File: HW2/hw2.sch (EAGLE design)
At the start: 22 parts, among them J1 USB-MINIB-5P

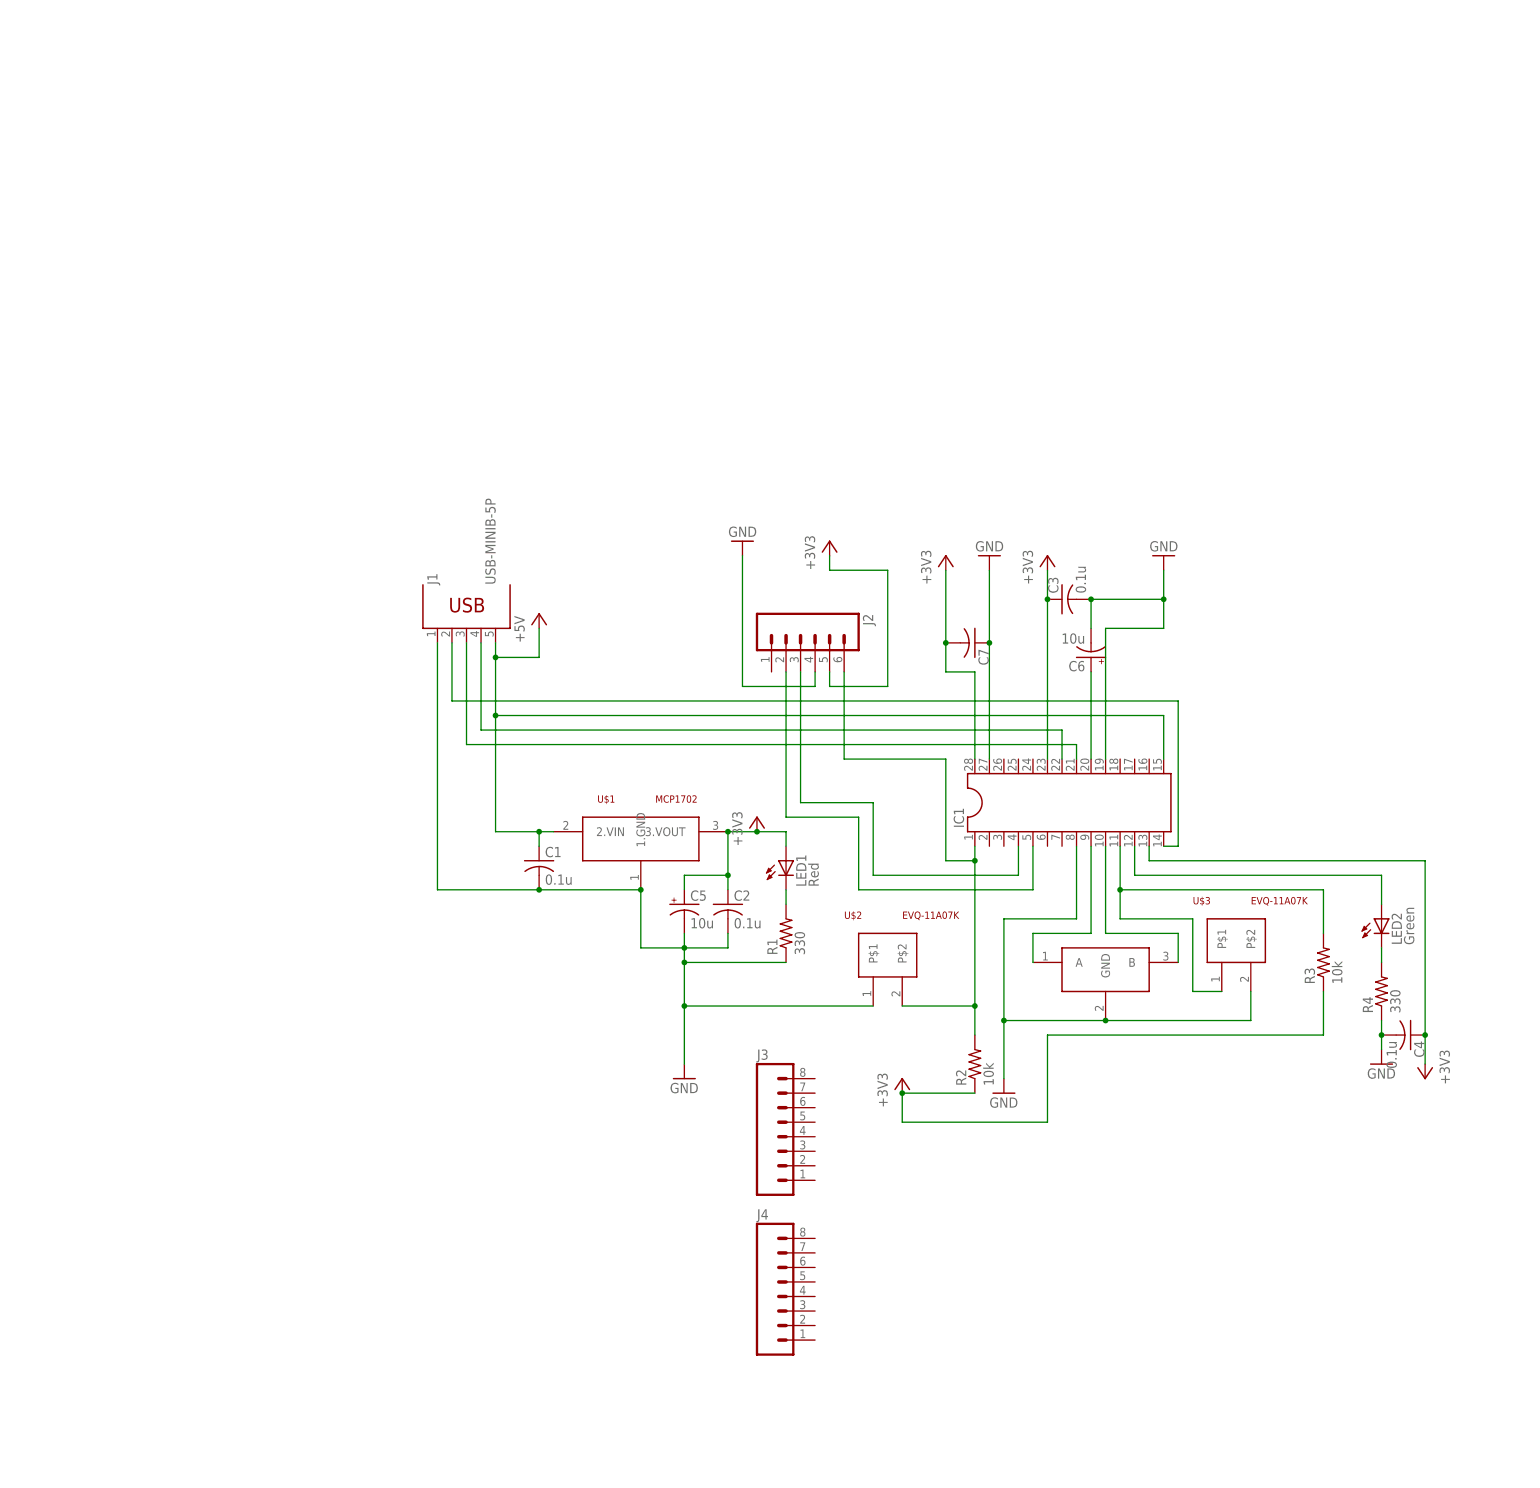
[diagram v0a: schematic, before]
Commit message: new schematic and library
The schematic has been improved.
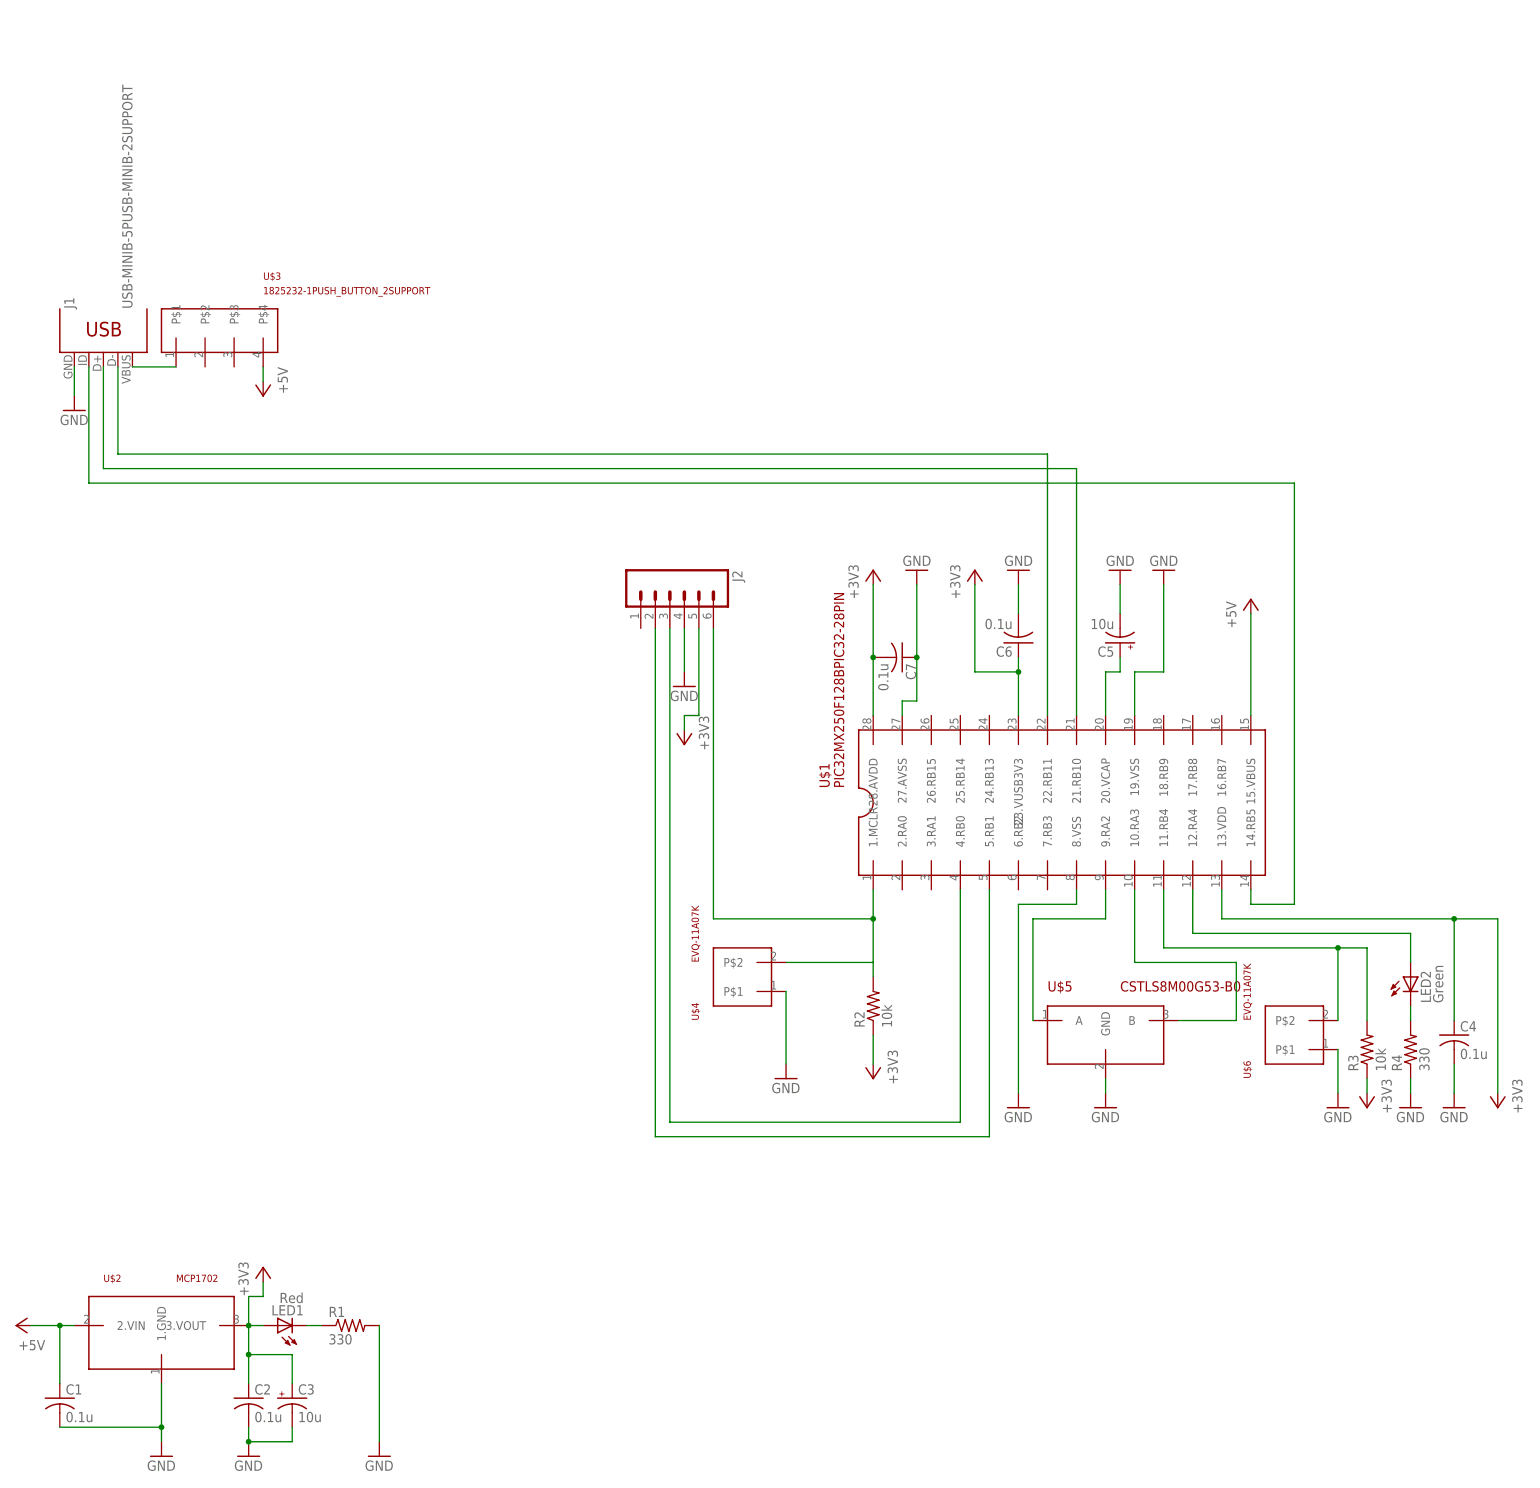
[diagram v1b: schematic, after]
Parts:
- removed IC1: (no value), hw2:DIL28-3
- removed J3, J4: (no value), hw2:M08
- added U$5: CSTLS8M00G53-B0, hw2:CSTLS8M00G53-B0
- added U$6: EVQ-11A07K, hw2:EVQ-11A07K
- C3: value 0.1u -> 10u; device hw2:C-US025-025X050 -> hw2:CPOL-USB45181A
- C6: value 10u -> 0.1u; device hw2:CPOL-USB45181A -> hw2:C-US025-025X050
- C7: value (none) -> 0.1u
- J1: value USB-MINIB-5P -> USB-MINIB-5PUSB-MINIB-2SUPPORT; device hw2:USB-MINIB-5P -> hw2:USB-MINIB-5PUSB-MINIB-2SUPPORT
- J2: device hw2:M06NO_SILK_YES_STOP -> hw2:M06SILK_FEMALE_PTH
- U$1: value MCP1702 -> PIC32MX250F128BPIC32-28PIN; device hw2:MCP1702 -> hw2:PIC32MX250F128BPIC32-28PIN
- U$2: value EVQ-11A07K -> MCP1702; device hw2:EVQ-11A07K -> hw2:MCP1702
- U$3: value EVQ-11A07K -> 1825232-1PUSH_BUTTON_2SUPPORT; device hw2:EVQ-11A07K -> hw2:1825232-1PUSH_BUTTON_2SUPPORT
- U$4: value CSTLS8M00G53-B0 -> EVQ-11A07K; device hw2:CSTLS8M00G53-B0 -> hw2:EVQ-11A07K
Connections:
- removed net N$15: IC1.10, U$4.B
- removed net N$16: IC1.11, R3.2, U$3.P$1
- removed net N$19: IC1.12, LED2.A
- new net N$1: J1.ID, U$1.14.RB5
- new net N$10: R3.2, U$1.11.RB4, U$6.P$2
- new net N$2: J1.D+, U$1.21.RB10
- new net N$6: J2.2, U$1.5.RB1
- net +3V3: now also C3.+, C6.1, U$1.13.VDD, U$1.23.VUSB3V3, U$1.28.AVDD, U$2.3.VOUT; no longer C3.1, C5.+, IC1.13, IC1.23, IC1.28, U$1.3.VOUT
- net +5V: now also U$1.15.VBUS, U$2.2.VIN, U$3.P$4; no longer IC1.15, J1.VBUS, U$1.2.VIN
- net GND: now also C3.-, C6.2, R1.2, U$1.19.VSS, U$1.27.AVSS, U$1.8.VSS, U$2.1.GND, U$4.P$1, U$5.GND, U$6.P$1; no longer C3.2, C6.-, IC1.19, IC1.27, IC1.8, R1.1, U$1.1.GND, U$2.P$1, U$3.P$2, U$4.GND
- net N$11: now also U$1.10.RA3, U$5.B; no longer IC1.5, J2.2
- net N$12: now also LED2.A, U$1.12.RA4; no longer IC1.4, J2.3
- net N$14: now also C5.+, U$1.20.VCAP; no longer IC1.9, U$4.A
- net N$3: now also LED1.C, R1.1; no longer IC1.22, J1.D-
- net N$4: now also J1.VBUS, U$3.P$1; no longer IC1.21, J1.D+
- net N$5: now also J1.D-, U$1.22.RB11; no longer IC1.14, J1.ID
- net N$7: now also J2.6, R2.2, U$1.1.MCLR, U$4.P$2; no longer C6.+, IC1.20
- net N$8: now also J2.3, U$1.4.RB0; no longer LED1.C, R1.2
- net N$9: now also U$1.9.RA2, U$5.A; no longer IC1.1, J2.6, R2.2, U$2.P$2
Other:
- moved on the sheet: C1, C2, C4, C5, C7, J1, J2, LED1, LED2, R1, R2, R3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

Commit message: brd file created
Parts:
- removed U$2: MCP1702, hw2:MCP1702
- removed U$3: 1825232-1PUSH_BUTTON_2SUPPORT, hw2:1825232-1PUSH_BUTTON_2SUPPORT
- added J3, J4: (no value), hw2:M08
- added SW3: 1825232-1PUSH_BUTTON_2SUPPORT, hw2:1825232-1PUSH_BUTTON_2SUPPORT
- added VR: MCP1702, hw2:MCP1702
- renumbered U$4 to RESET_BUTTON, U$5 to CR, U$6 to USER_BUTTON
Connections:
- new net N$15: J3.1, U$1.2.RA0
- new net N$16: J3.2, U$1.3.RA1
- new net N$17: J3.3, U$1.6.RB2
- new net N$18: J3.4, U$1.7.RB3
- new net N$19: J4.1, U$1.26.RB15
- new net N$20: J4.2, U$1.25.RB14
- new net N$21: J4.3, U$1.24.RB13
- new net N$22: J4.4, U$1.18.RB9
- new net N$23: J4.5, U$1.17.RB8
- new net N$24: J4.6, U$1.16.RB7
- net +3V3: now also J3.7, VR.3.VOUT; no longer U$2.3.VOUT
- net +5V: now also J4.7, SW3.P$4, VR.2.VIN; no longer U$2.2.VIN, U$3.P$4
- net GND: now also J3.8, J4.8, VR.1.GND; no longer U$2.1.GND
- net N$10: now also J3.5
- net N$12: now also J3.6
- net N$4: now also SW3.P$1; no longer U$3.P$1
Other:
- moved on the sheet: C1, C2, C3, J1, LED1, R1
